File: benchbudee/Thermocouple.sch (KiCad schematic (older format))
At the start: 20 parts, among them P2 CONN_2, P3 CONN_3X2, U2 MCP3901, U3 LMT84, U4 OPA4170

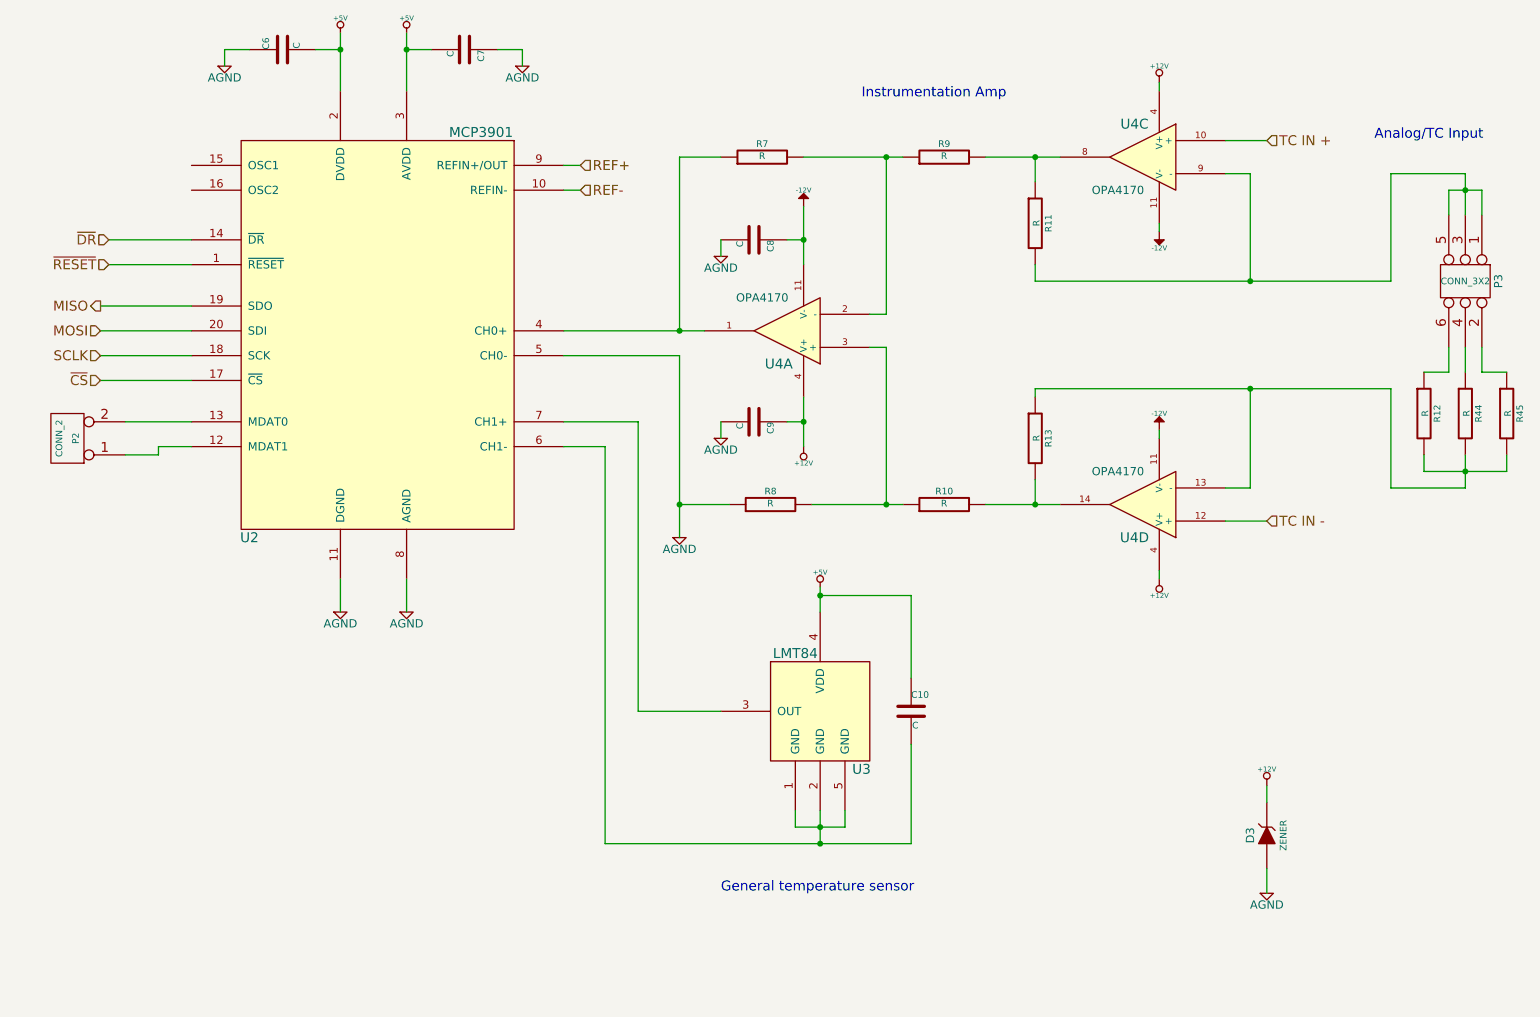
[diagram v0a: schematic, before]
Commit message: Initial placement of thermocouple module
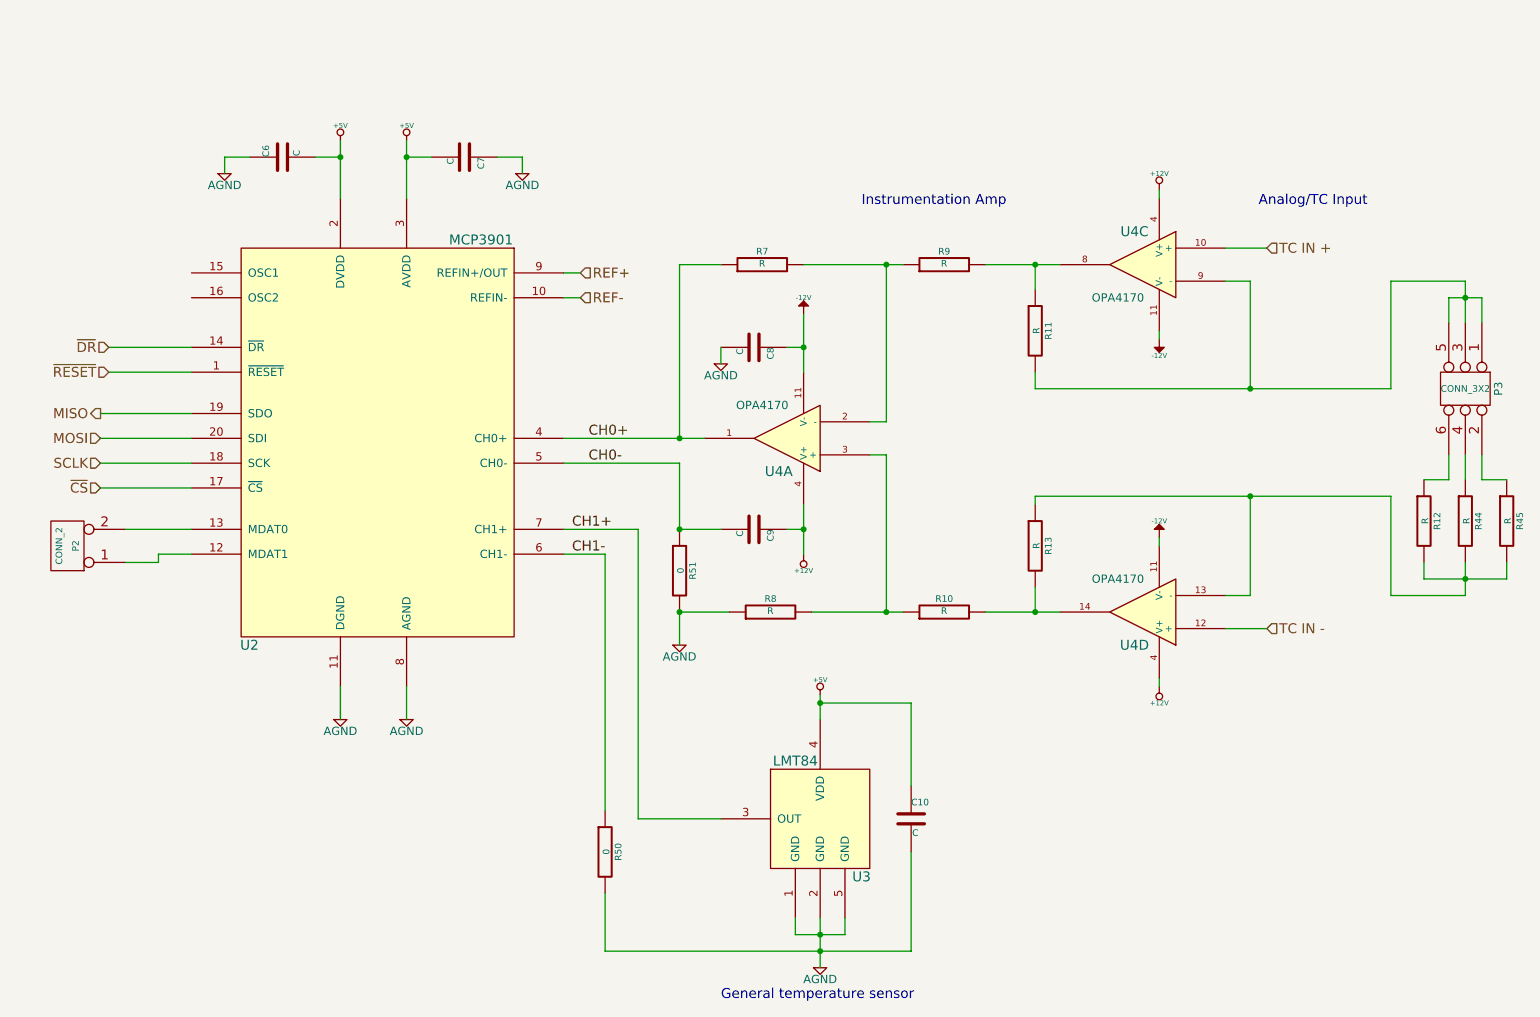
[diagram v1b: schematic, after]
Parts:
- removed D3: ZENER, ~, symbol ZENER
- added R50, R51: 0, ~, symbol R
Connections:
- net AGND: now also C10.2, U3.1 (GND), U3.2 (GND), U3.5 (GND), R50.2, R51.2; no longer C9.2, U2.5 (CH0-)
- net CH0+: now reaches R7.1, U2.4 (CH0+), U4.1
- net CH1+: now reaches U2.7 (CH1+), U3.3 (OUT)
- new net CH0-: C9.2, R51.1, U2.5 (CH0-)
- new net CH1-: R50.1, U2.6 (CH1-)
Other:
- moved on the sheet: C10, C6, C7, C8, C9, P2, P3, R10, R11, R12, R13, R44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
